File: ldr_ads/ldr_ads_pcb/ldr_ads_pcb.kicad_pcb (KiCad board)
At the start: 2 copper layers, 21 x 23 mm, 5 parts, among them J1 Conn_01x03

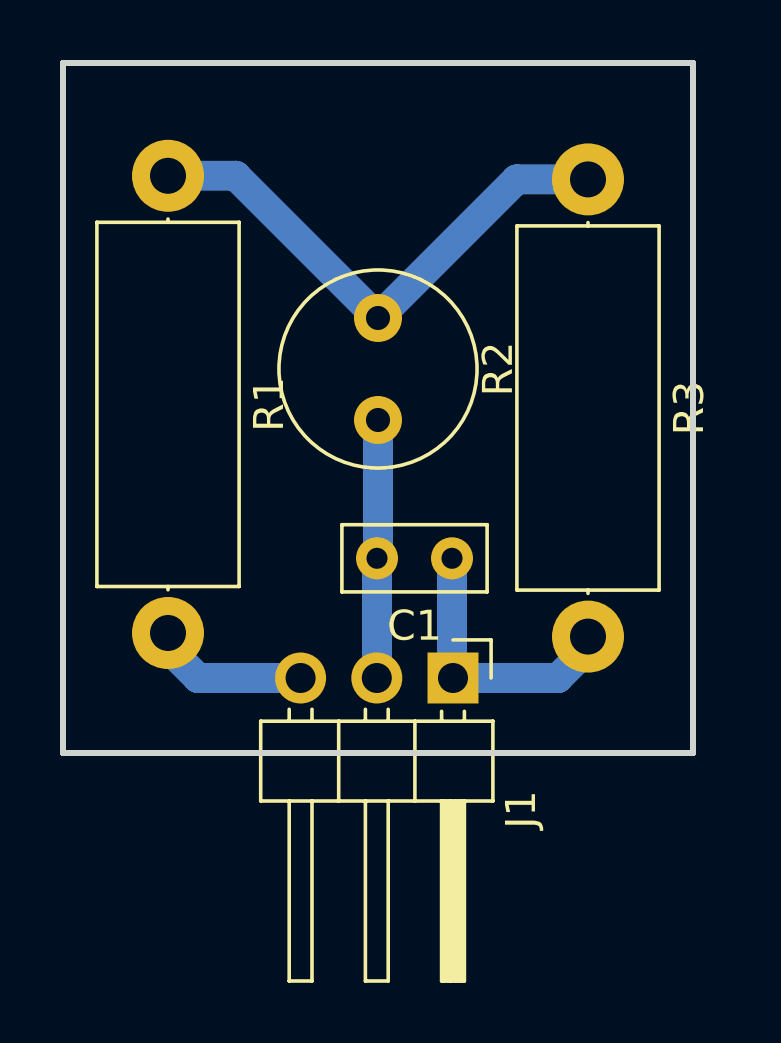
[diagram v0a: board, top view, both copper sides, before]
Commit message: changed ldr pcb
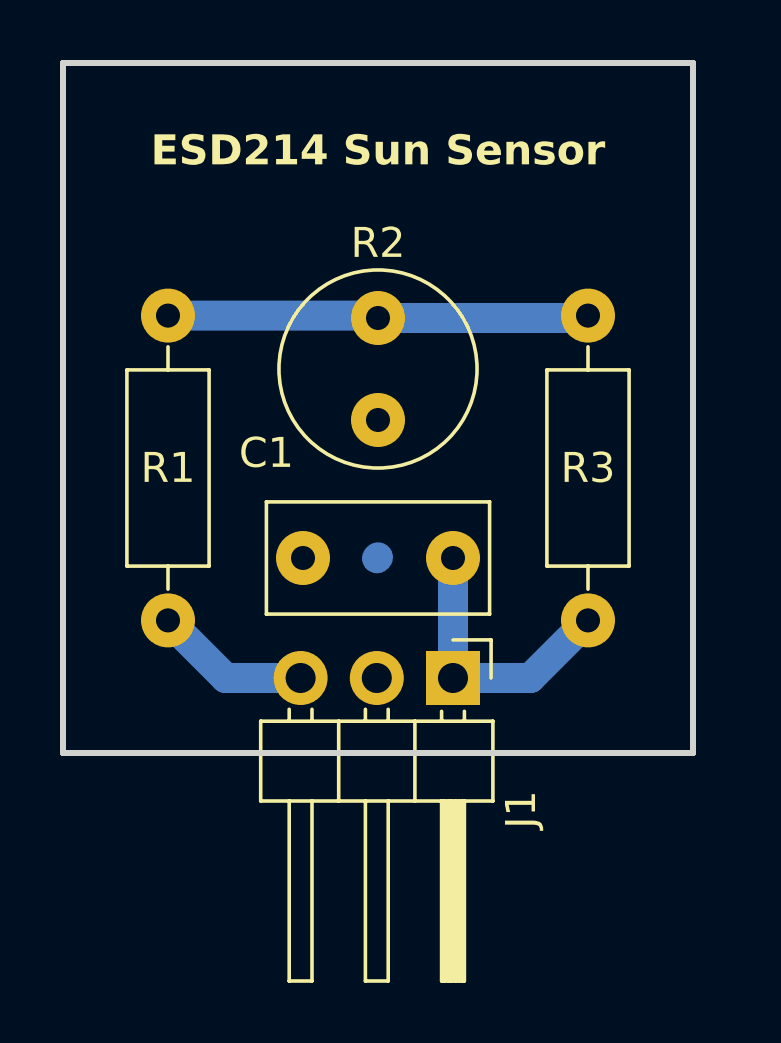
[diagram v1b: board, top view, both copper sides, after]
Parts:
- C1: footprint Capacitor_THT:C_Rect_L4.6mm_W2.0mm_P2.50mm_MKS02_FKP02 -> Capacitor_THT:C_Rect_L7.2mm_W3.5mm_P5.00mm_FKS2_FKP2_MKS2_MKP2
- R1, R3: footprint Resistor_THT:R_Axial_DIN0414_L11.9mm_D4.5mm_P15.24mm_Horizontal -> Resistor_THT:R_Axial_DIN0207_L6.3mm_D2.5mm_P10.16mm_Horizontal
- moved R1 14.8 mm to (39.0, 43.1), turned to 90 degrees
- moved R3 4.54 mm to (53.0, 32.9)
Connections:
- R1 pad 1: Net-(R1-Pad1) -> +3.3V
- R1 pad 2: +3.3V -> Net-(R1-Pad2)
- R2 pad 1: Net-(R1-Pad1) -> Net-(R1-Pad2)
- R3 pad 1: Net-(R1-Pad1) -> Net-(R1-Pad2)
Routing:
- net Net-(R1-Pad1): track 18.0 -> 0.00 mm
- net Net-(R1-Pad2): track 0.00 -> 14.1 mm
- net GND: track 8.63 -> 0.06 mm
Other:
- board text added: "3.3V"
- board text added: "ESD214 Sun Sensor"
- board text added: "Out"

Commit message: last inderation of ldr_sensor
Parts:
- moved R1 0.92 mm to (39.0, 42.2)
- moved R3 0.92 mm to (53.0, 32.0)
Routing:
- net +3.3V: track 5.22 -> 6.38 mm
- net /out: track 9.34 -> 10.5 mm
- net Net-(R1-Pad2): track 14.1 -> 14.8 mm
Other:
- board size 21 x 23 mm -> 20.5 x 22 mm
